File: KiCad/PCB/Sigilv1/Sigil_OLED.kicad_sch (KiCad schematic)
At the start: 6 parts, among them J2 INLAND 1.3" OLED HEADER (7-PI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, J3 BUZZER LOGICAL ONLY, J4 FIVE-BUTTON D-PAD, J5 NEOPIXEL JEWEL 7 RGBW, U1 REMOVABLE ESP32 DEVKIT / 2 x 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

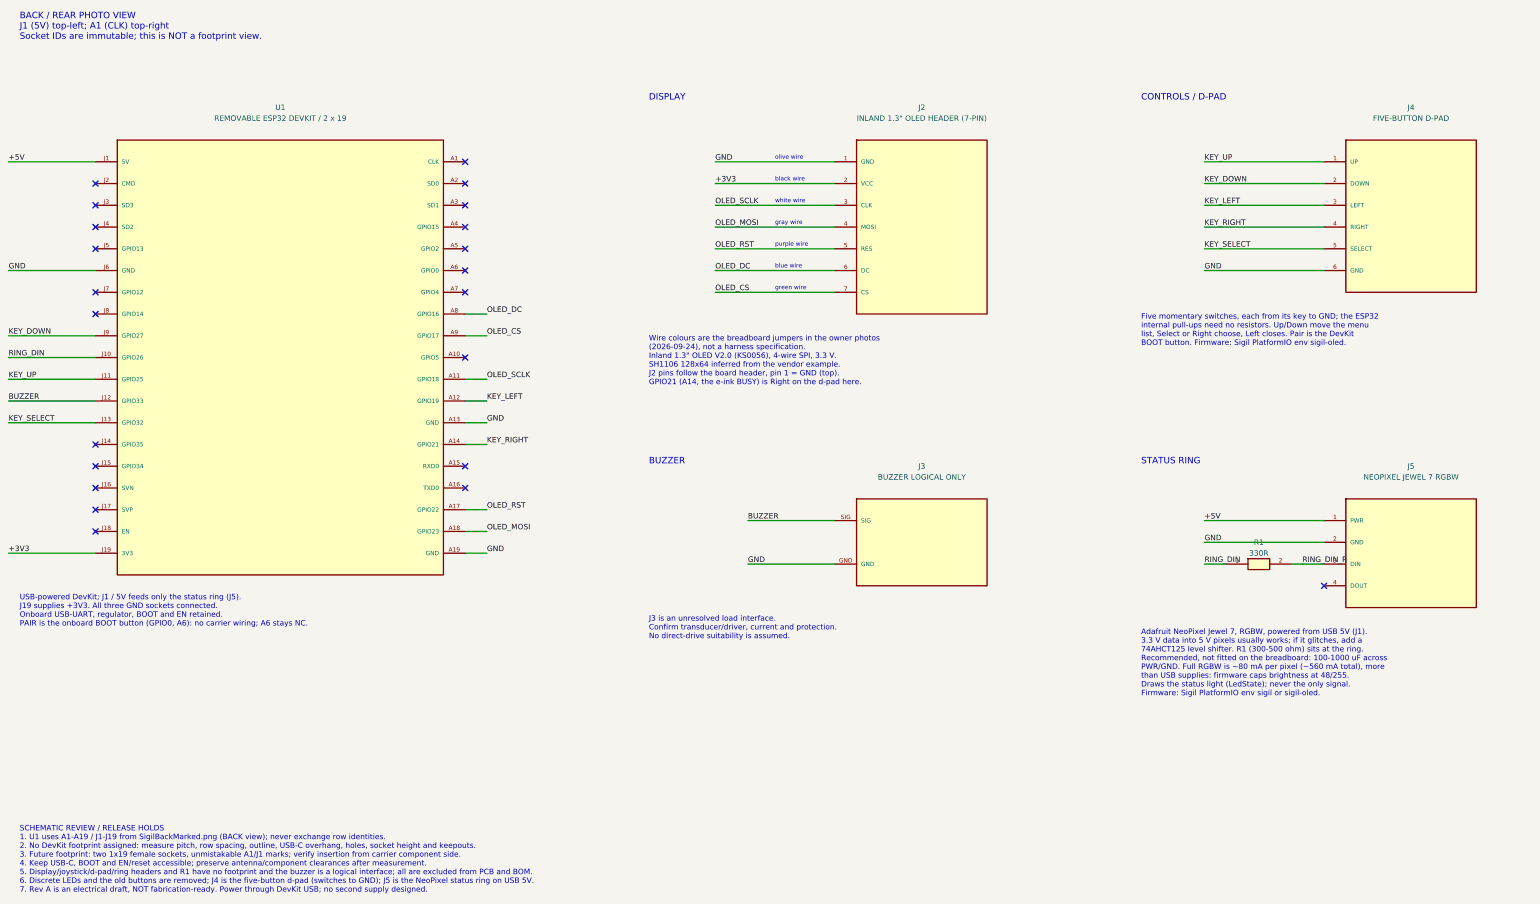
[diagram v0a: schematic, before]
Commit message: OLED Sigil schematic: five discrete pushbuttons replace the d-pad header
J4 (a d-pad module header) becomes SW1-SW5, momentary pushbuttons from
each key GPIO to a shared GND with the internal pull-ups: Up J11/GPIO25,
Down J9/GPIO27, Left A12/GPIO19, Right A14/GPIO21, Select J13/GPIO32.
Firmware already reads them this way. Rebuilt with build_schematic.py;
verify_schematic.py passes and KiCad ERC reports 0 violations on both
schematics.

Co-Authored-By: Claude Opus 5.5 <noreply@anthropic.com>
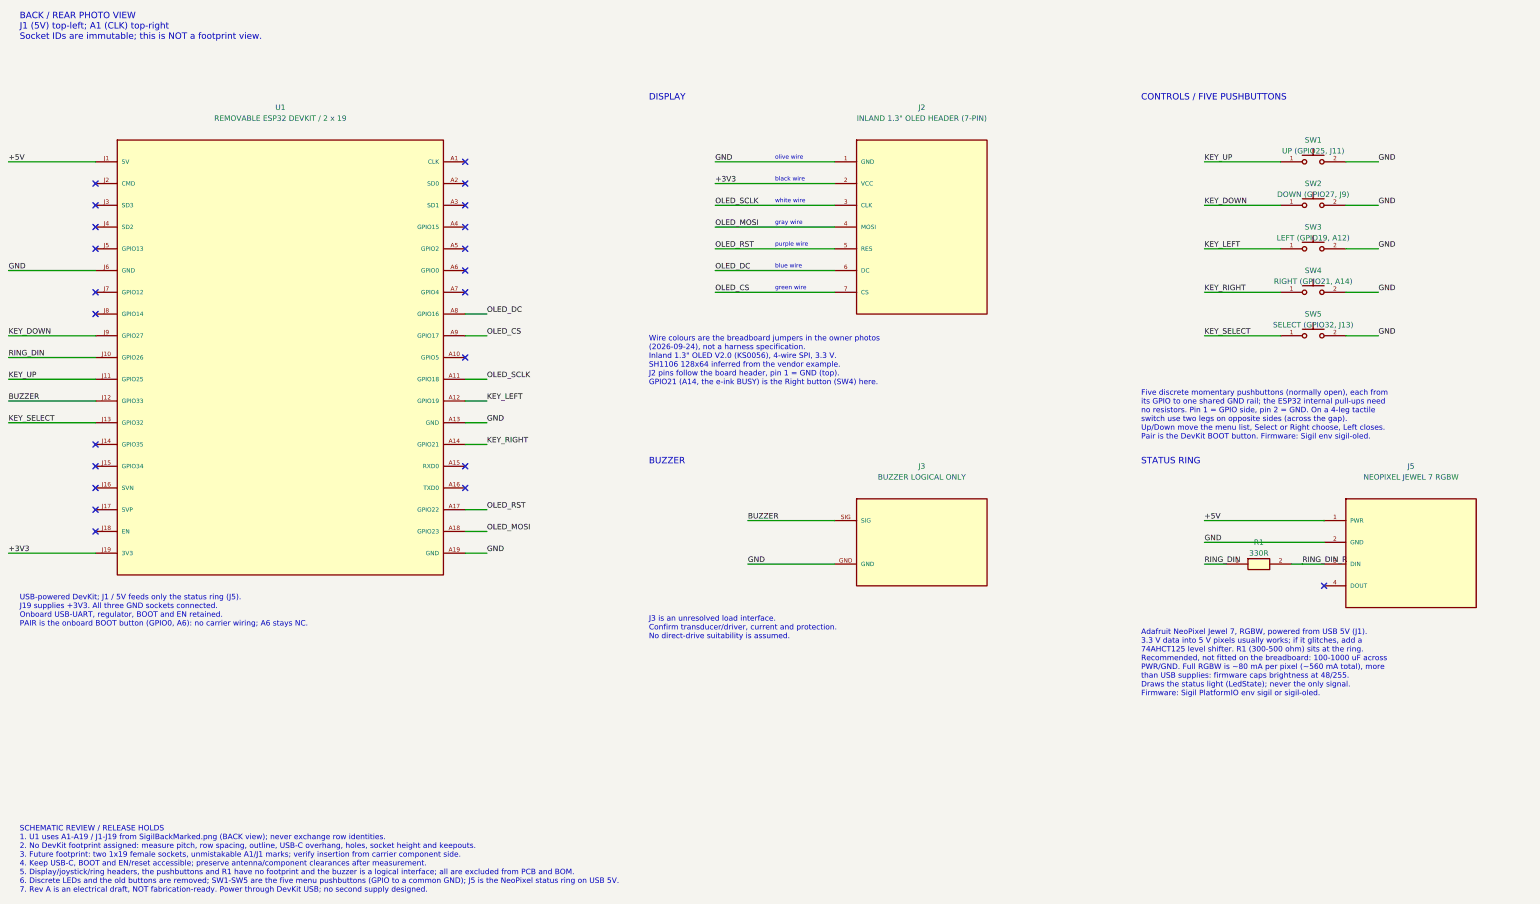
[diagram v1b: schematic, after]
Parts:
- removed J4: FIVE-BUTTON D-PAD, symbol Sigil:DPad_5_Key_Header
- added SW1: UP (GPIO25, J11), symbol Sigil:Pushbutton_SPST_NO
- added SW2: DOWN (GPIO27, J9), symbol Sigil:Pushbutton_SPST_NO
- added SW3: LEFT (GPIO19, A12), symbol Sigil:Pushbutton_SPST_NO
- added SW4: RIGHT (GPIO21, A14), symbol Sigil:Pushbutton_SPST_NO
- added SW5: SELECT (GPIO32, J13), symbol Sigil:Pushbutton_SPST_NO
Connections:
- net GND: now also SW1.2, SW2.2, SW3.2, SW4.2, SW5.2
- net KEY_DOWN: now also SW2.1
- net KEY_LEFT: now also SW3.1
- net KEY_RIGHT: now also SW4.1
- net KEY_SELECT: now also SW5.1
- net KEY_UP: now also SW1.1
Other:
- note added: "CONTROLS / FIVE PUSHBUTTONS"
- note added: "Five discrete momentary pushbuttons (normally open), each from its GPIO to one shared GND rail; the ESP32 internal pull-ups need no resistors. Pin 1 = GPIO side, pin 2 = GND. On a 4-leg tactile switch use two legs on opposite sides (across the gap). Up/Down move the menu list, Select or Right choose, Left closes. Pair is the DevKit BOOT button. Firmware: Sigil env sigil-oled."
- note added: "Wire colours are the breadboard jumpers in the owner photos (2026-09-24), not a harness specification. Inland 1.3" OLED V2.0 (KS0056), 4-wire SPI, 3.3 V. SH1106 128x64 inferred from the vendor example. J2 pins follow the board header, pin 1 = GND (top). GPIO21 (A14, the e-ink BUSY) is the Right button (SW4) here."
- note removed: "CONTROLS / D-PAD"
- note removed: "Five momentary switches, each from its key to GND; the ESP32 internal pull-ups need no resistors. Up/Down move the menu list, Select or Right choose, Left closes. Pair is the DevKit BOOT button. Firmware: Sigil PlatformIO env sigil-oled."
- note removed: "Wire colours are the breadboard jumpers in the owner photos (2026-09-24), not a harness specification. Inland 1.3" OLED V2.0 (KS0056), 4-wire SPI, 3.3 V. SH1106 128x64 inferred from the vendor example. J2 pins follow the board header, pin 1 = GND (top). GPIO21 (A14, the e-ink BUSY) is Right on the d-pad here."

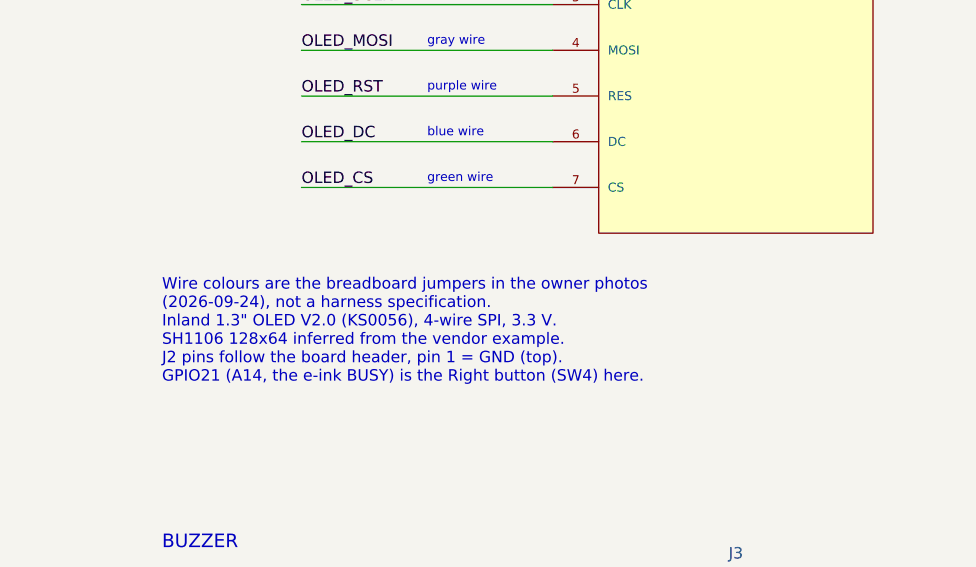
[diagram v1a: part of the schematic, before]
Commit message: Turntest notes: softer white, OLED key help, pass countdown, living heart, US spellings
- Jewel: full RGB white (hold fill, starter, lobby invite) is now a soft
  warm white; it was glaring next to every other cue.
- OLED game screen: one line of key help under the life total
  ("<> life  press: menu", or "Click again to undo" while passing).
- Pending pass: Sigils show PASSING and a green ring countdown while
  Undo pass is on offer; a second Select on the OLED undoes the pass.
  Atlas's screen counts down "Passing in Ns". PASS_GRACE_MS moves to
  protocol.h so both firmwares share it; Atlas still owns the timer.
- Life heart: new StartingLife packet (37, Atlas -> menu Sigils, resent
  with Hello; older Sigils ignore it). The heart drains from the top below
  the starting life and grows up to 1.5x at double it.
- US spellings in UI text, comments, docs, KiCad notes and manual V0.3.
  Wire tokens (CANCELLED) and code identifiers are unchanged.

Co-Authored-By: Claude Opus 5.5 <noreply@anthropic.com>
Claude-Session: https://claude.ai/code/session_019MjMMnFUjQwKLv4TjtKLwb
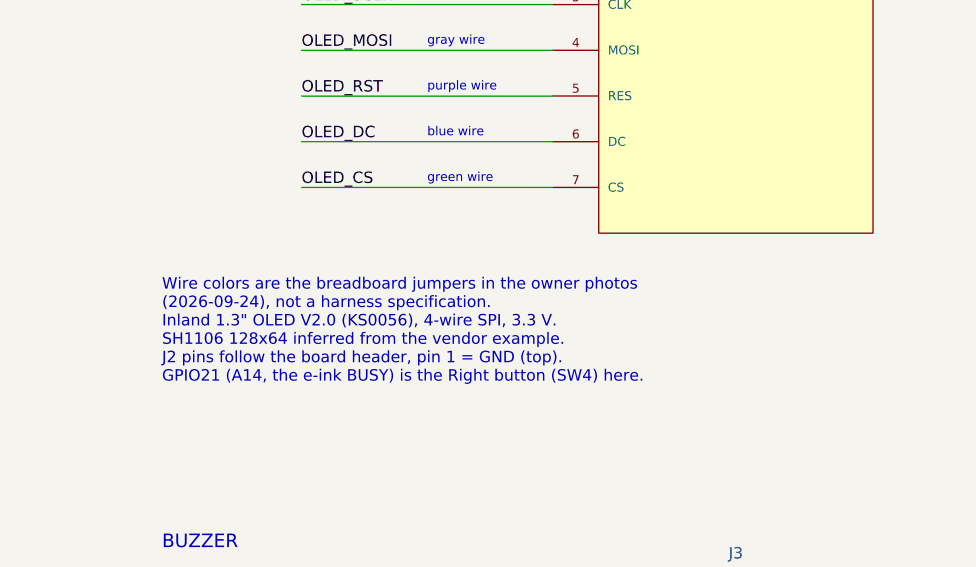
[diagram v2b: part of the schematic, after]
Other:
- note added: "Wire colors are the breadboard jumpers in the owner photos (2026-09-24), not a harness specification. Inland 1.3" OLED V2.0 (KS0056), 4-wire SPI, 3.3 V. SH1106 128x64 inferred from the vendor example. J2 pins follow the board header, pin 1 = GND (top). GPIO21 (A14, the e-ink BUSY) is the Right button (SW4) here."
- note removed: "Wire colours are the breadboard jumpers in the owner photos (2026-09-24), not a harness specification. Inland 1.3" OLED V2.0 (KS0056), 4-wire SPI, 3.3 V. SH1106 128x64 inferred from the vendor example. J2 pins follow the board header, pin 1 = GND (top). GPIO21 (A14, the e-ink BUSY) is the Right button (SW4) here."
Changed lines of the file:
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@@
 		(comment 1 "Rear-photo socket numbering. Buttons SW1-SW5, status ring J5.")
 	)
-	(text "Wire colours are the breadboard jumpers in the owner photos\n(2026-09-24), not a harness specification.\nInland 1.3\" OLED V2.0 (KS0056), 4-wire SPI, 3.3 V.\nSH1106 128x64 inferred from the vendor example.\nJ2 pins follow the board header, pin 1 = GND (top).\nGPIO21 (A14, the e-ink BUSY) is the Right button (SW4) here."
+	(text "Wire colors are the breadboard jumpers in the owner photos\n(2026-09-24), not a harness specification.\nInland 1.3\" OLED V2.0 (KS0056), 4-wire SPI, 3.3 V.\nSH1106 128x64 inferred from the vendor example.\nJ2 pins follow the board header, pin 1 = GND (top).\nGPIO21 (A14, the e-ink BUSY) is the Right button (SW4) here."
 		(exclude_from_sim no)
 		(at 175 96.52 0)

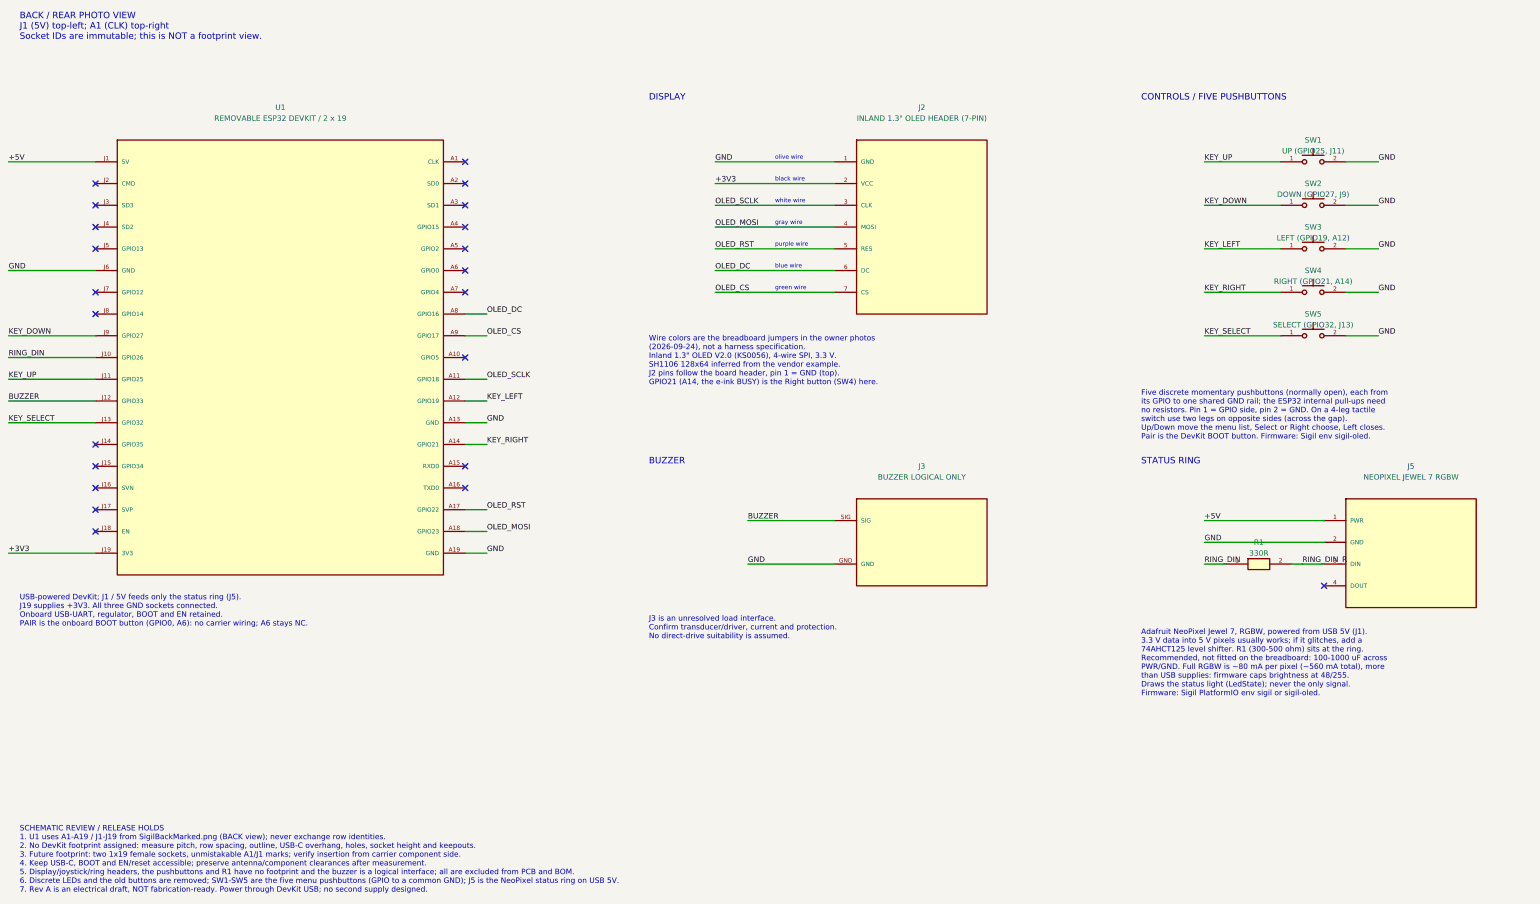
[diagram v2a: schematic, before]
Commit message: Sigil schematics: first-PCB footprints, GPIO4 display strap, ring and 3V3 capacitors
- Every carrier part except the DevKit (U1) gets a through-hole footprint
  and joins the BOM; J3 becomes a numbered 2-pin buzzer header.
- A7/GPIO4 strap: open on the E-ink board, GND on the OLED board, matching
  HW_TYPE_STRAP_PIN (the OLED draft had it NC, which would halt at boot).
- C1 470 uF across the Jewel supply, C2 10 uF on +3V3.
- tools/offline_netlist.py lets verify_schematic.py run without KiCad;
  ERC still needs a KiCad re-run.

Co-Authored-By: Claude Opus 5.5 <noreply@anthropic.com>
Claude-Session: https://claude.ai/code/session_01EuTMd98XaCZ1DRqGGQFyaV
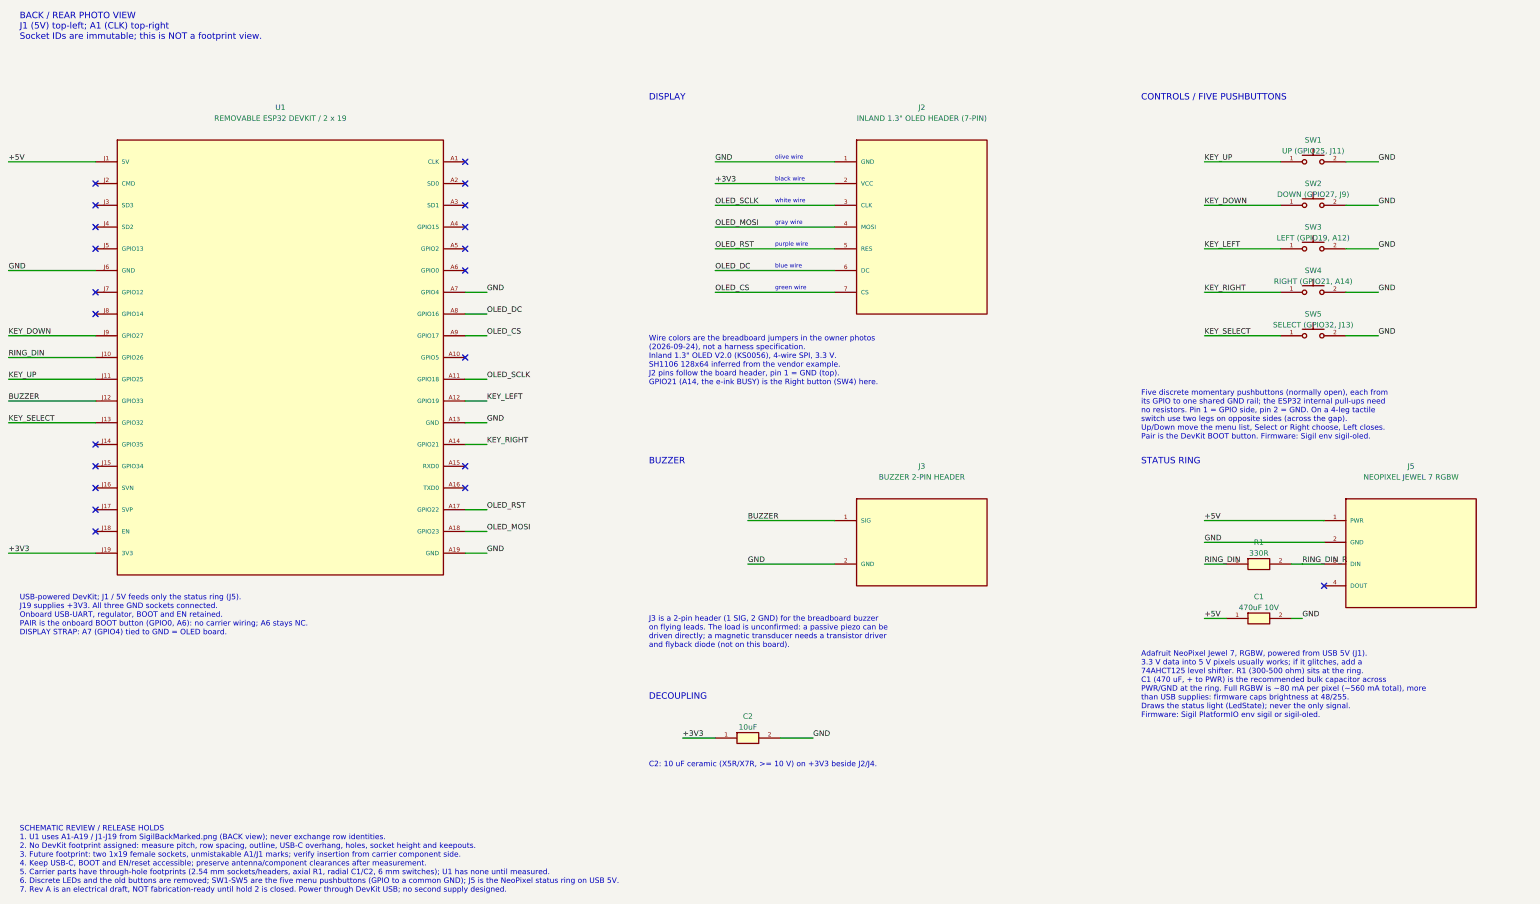
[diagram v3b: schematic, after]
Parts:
- added C1: 470uF 10V, Capacitor_THT:CP_Radial_D8.0mm_P3.50mm, symbol Sigil:Capacitor
- added C2: 10uF, Capacitor_THT:C_Disc_D5.0mm_W2.5mm_P5.00mm, symbol Sigil:Capacitor
- J2: footprint (none) -> Connector_PinSocket_2.54mm:PinSocket_1x07_P2.54mm_Vertical; now in the parts list
- J3: value BUZZER LOGICAL ONLY -> BUZZER 2-PIN HEADER; footprint (none) -> Connector_PinHeader_2.54mm:PinHeader_1x02_P2.54mm_Vertical; now in the parts list
- J5: footprint (none) -> Connector_PinHeader_2.54mm:PinHeader_1x04_P2.54mm_Vertical; now in the parts list
- R1: footprint (none) -> Resistor_THT:R_Axial_DIN0207_L6.3mm_D2.5mm_P7.62mm_Horizontal; now in the parts list
- SW1, SW2, SW3, SW4, SW5: footprint (none) -> Button_Switch_THT:SW_PUSH_6mm; now in the parts list
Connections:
- net +3V3: now also C2.1
- net +5V: now also C1.1
- net BUZZER: now also J3.1 (SIG); no longer J3.SIG
- net GND: now also J3.2 (GND), U1.A7 (GPIO4), C1.2, C2.2; no longer J3.GND
- no-connect marks 22 -> 21
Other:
- note added: "Adafruit NeoPixel Jewel 7, RGBW, powered from USB 5V (J1). 3.3 V data into 5 V pixels usually works; if it glitches, add a 74AHCT125 level shifter. R1 (300-500 ohm) sits at the ring. C1 (470 uF, + to PWR) is the recommended bulk capacitor across PWR/GND at the ring. Full RGBW is ~80 mA per pixel (~560 mA total), more than USB supplies: firmware caps brightness at 48/255. Draws the status light (L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"
- note added: "C2: 10 uF ceramic (X5R/X7R, >= 10 V) on +3V3 beside J2/J4."
- note added: "DECOUPLING"
- note added: "J3 is a 2-pin header (1 SIG, 2 GND) for the breadboard buzzer on flying leads. The load is unconfirmed: a passive piezo can be driven directly; a magnetic transducer needs a transistor driver and flyback diode (not on this board)."
- note added: "USB-powered DevKit; J1 / 5V feeds only the status ring (J5). J19 supplies +3V3. All three GND sockets connected. Onboard USB-UART, regulator, BOOT and EN retained. PAIR is the onboard BOOT button (GPIO0, A6): no carrier wiring; A6 stays NC. DISPLAY STRAP: A7 (GPIO4) tied to GND = OLED board."
- note removed: "Adafruit NeoPixel Jewel 7, RGBW, powered from USB 5V (J1). 3.3 V data into 5 V pixels usually works; if it glitches, add a 74AHCT125 level shifter. R1 (300-500 ohm) sits at the ring. Recommended, not fitted on the breadboard: 100-1000 uF across PWR/GND. Full RGBW is ~80 mA per pixel (~560 mA total), more than USB supplies: firmware caps brightness at 48/255. Draws the status light (LedState); nev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"
- note removed: "J3 is an unresolved load interface. Confirm transducer/driver, current and protection. No direct-drive suitability is assumed."
- note removed: "USB-powered DevKit; J1 / 5V feeds only the status ring (J5). J19 supplies +3V3. All three GND sockets connected. Onboard USB-UART, regulator, BOOT and EN retained. PAIR is the onboard BOOT button (GPIO0, A6): no carrier wiring; A6 stays NC."
